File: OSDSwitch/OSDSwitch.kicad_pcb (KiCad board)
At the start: 2 copper layers, 25.4 x 33 mm, 15 parts, among them IC1 ADG1633BCPZ-REEL7, J1 Conn_01x03_Pin, J2 Conn_01x03_Pin, J3 Conn_01x03_Pin, J4 Conn_01x05, J5 Conn_01x04, J6 Conn_01x02

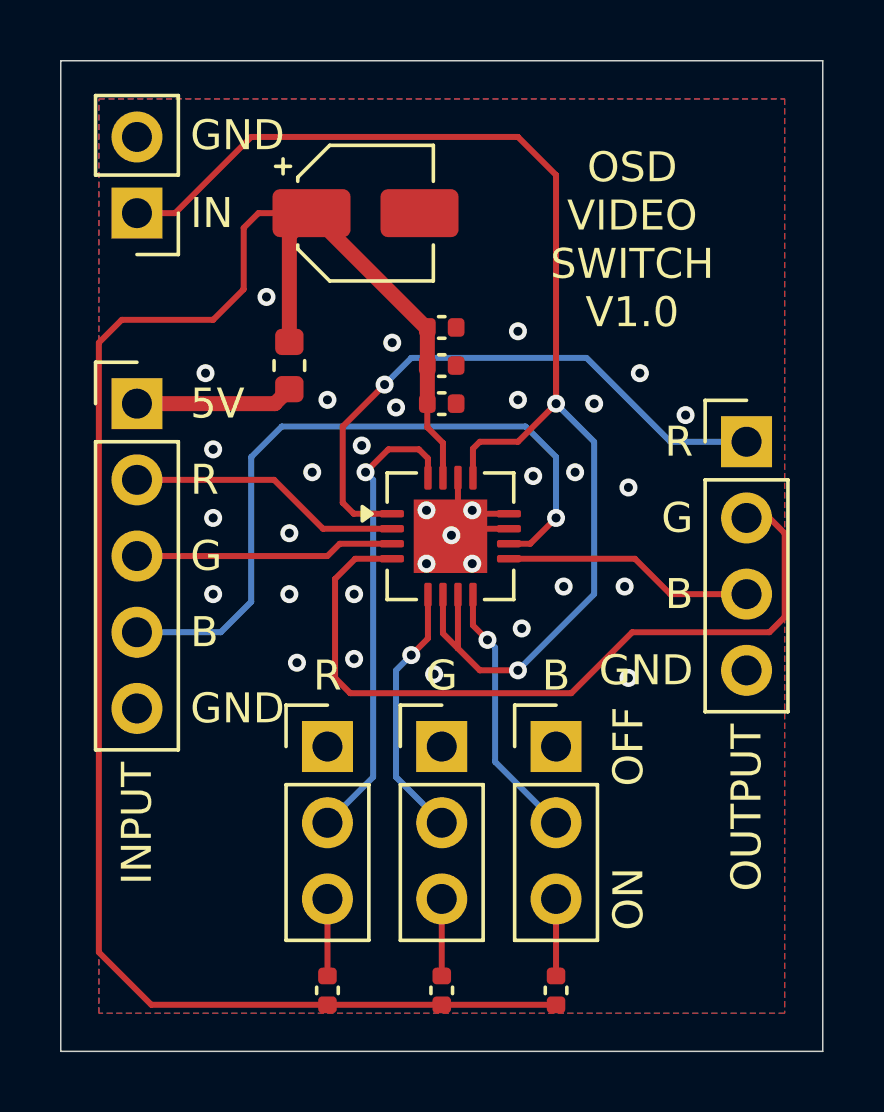
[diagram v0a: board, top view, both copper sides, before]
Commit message: Corrected chip footprint
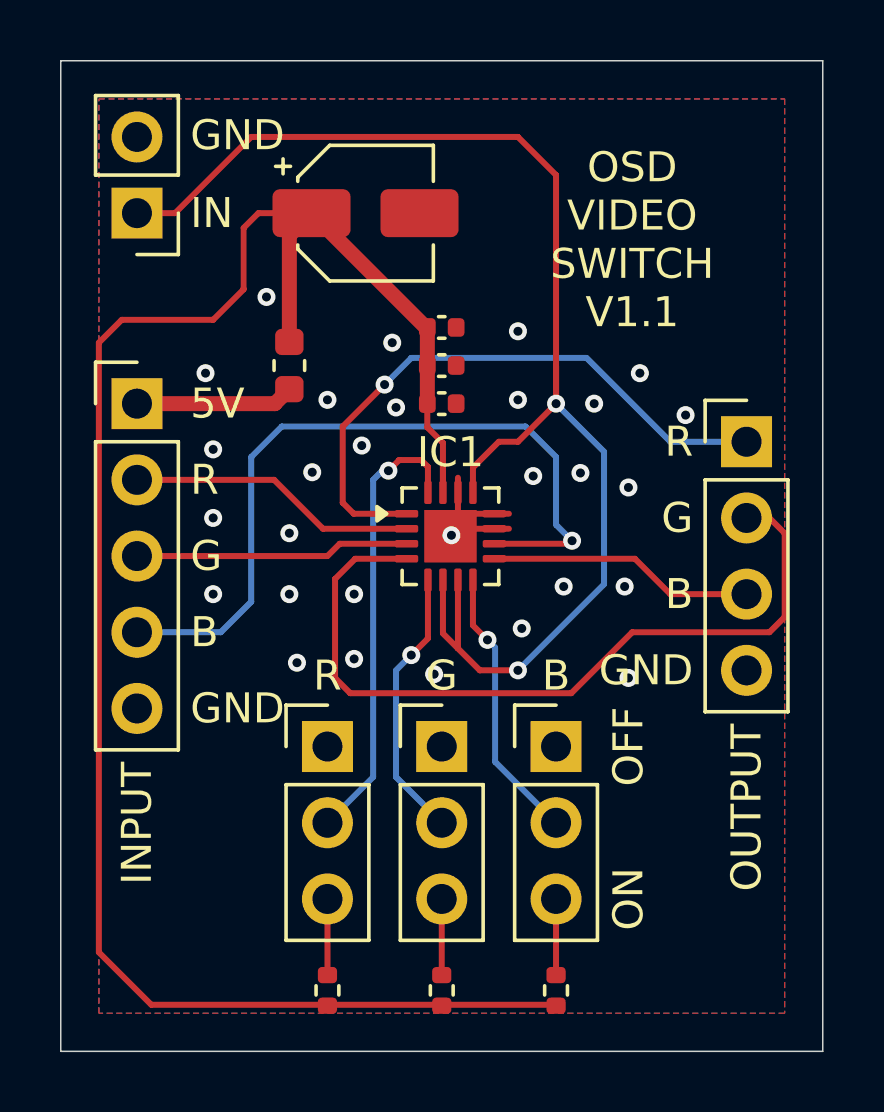
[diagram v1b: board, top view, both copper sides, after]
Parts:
- C4: value 1uF -> 1uF/16V
- IC1: footprint Package_DFN_QFN:QFN-16-1EP_4x4mm_P0.5mm_EP2.45x2.45mm -> Package_DFN_QFN:QFN-16-1EP_3x3mm_P0.5mm_EP1.75x1.75mm
- J1, J3: value Conn_01x03_Pin -> Conn_01x03_Pin_J12
- J2: value Conn_01x03_Pin -> Conn_01x03_Pin_J23
- R1, R2, R3: footprint Capacitor_SMD:C_0402_1005Metric -> Resistor_SMD:R_0402_1005Metric
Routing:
- net /BLUE_IN: track 24.3 -> 26.0 mm
- net /OSD_VID: track 45.4 -> 46.7 mm
- net +5V: track 62.1 -> 63.0 mm
- net GND: vias 33 -> 29
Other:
- board text added: "OSD VIDEO SWITCH V1.1"
- board text removed: "OSD VIDEO SWITCH V1.0"

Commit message: Swapped red and blue to match Amiga 500 video output order
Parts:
- R1, R2, R3: value 470R -> 330R
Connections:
- IC1 pad 1: /RED_OUT -> /BLUE_OUT
- IC1 pad 10: /BLUE_IN -> /RED_IN
- IC1 pad 2: /RED_IN -> /BLUE_IN
- IC1 pad 9: /BLUE_OUT -> /RED_OUT
- J4 pad 2: /RED_IN -> /BLUE_IN
- J4 pad 4: /BLUE_IN -> /RED_IN
- J5 pad 1: /RED_OUT -> /BLUE_OUT
- J5 pad 3: /BLUE_OUT -> /RED_OUT
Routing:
- net /RED_IN: track 9.66 -> 26.0 mm, vias 0 -> 1
- net /BLUE_IN: track 26.0 -> 9.66 mm, vias 1 -> 0
- net /RED_OUT: track 20.4 -> 8.90 mm, vias 1 -> 0
- net /BLUE_OUT: track 8.90 -> 20.4 mm, vias 0 -> 1
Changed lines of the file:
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@@
 			(layers "*.Cu" "*.Mask")
 			(remove_unused_layers no)
-			(net 4 "/RED_IN")
+			(net 12 "/BLUE_IN")
 			(pinfunction "Pin_2")
 			(pintype "passive")
@@
 			(layers "*.Cu" "*.Mask")
 			(remove_unused_layers no)
-			(net 12 "/BLUE_IN")
+			(net 4 "/RED_IN")
 			(pinfunction "Pin_4")
 			(pintype "passive")
@@
 			)
 		)
-		(property "Value" "470R"
+		(property "Value" "330R"
 			(at 0 1.17 90)
 			(layer "F.Fab")
@@
 			)
 		)
-		(property "Value" "470R"
+		(property "Value" "330R"
 			(at 0 1.17 90)
 			(layer "F.Fab")
@@
 			(layers "*.Cu" "*.Mask")
 			(remove_unused_layers no)
-			(net 11 "/RED_OUT")
+			(net 5 "/BLUE_OUT")
 			(pinfunction "Pin_1")
 			(pintype "passive")
@@
 			(layers "*.Cu" "*.Mask")
 			(remove_unused_layers no)
-			(net 5 "/BLUE_OUT")
+			(net 11 "/RED_OUT")
 			(pinfunction "Pin_3")
 			(pintype "passive")
@@
 			)
 		)
-		(property "Value" "470R"
+		(property "Value" "330R"
 			(at 0 1.17 90)
 			(layer "F.Fab")
@@
 			(layers "F.Cu" "F.Mask" "F.Paste")
 			(roundrect_rratio 0.25)
-			(net 11 "/RED_OUT")
+			(net 5 "/BLUE_OUT")
 			(pinfunction "D1")
 			(pintype "passive")
@@
 			(layers "F.Cu" "F.Mask" "F.Paste")
 			(roundrect_rratio 0.25)
-			(net 4 "/RED_IN")
+			(net 12 "/BLUE_IN")
 			(pinfunction "S1B")
 			(pintype "passive")
@@
 			(layers "F.Cu" "F.Mask" "F.Paste")
 			(roundrect_rratio 0.25)
-			(net 5 "/BLUE_OUT")
+			(net 11 "/RED_OUT")
 			(pinfunction "D3")
 			(pintype "passive")
@@
 			(layers "F.Cu" "F.Mask" "F.Paste")
 			(roundrect_rratio 0.25)
-			(net 12 "/BLUE_IN")
+			(net 4 "/RED_IN")
 			(pinfunction "S3B")
 			(pintype "passive")
@@
 	)
 	(gr_text "R"
-		(at 173.482 91.44 0)
+		(at 173.5074 96.52 0)
 		(layer "F.SilkS")
 		(effects
@@
 	)
 	(gr_text "B"
-		(at 173.482 96.52 0)
+		(at 173.5074 91.44 0)
 		(layer "F.SilkS")
 		(effects
@@
 	)
 	(gr_text "B"
-		(at 168.91 99.822 0)
+		(at 161.29 99.822 0)
 		(layer "F.SilkS")
 		(effects
@@
 	)
 	(gr_text "B"
-		(at 156.718 97.79 0)
+		(at 156.718 92.71 0)
 		(layer "F.SilkS")
 		(effects
@@
 	)
 	(gr_text "R"
-		(at 161.29 99.822 0)
+		(at 168.91 99.822 0)
 		(layer "F.SilkS")
 		(effects
@@
 	)
 	(gr_text "R"
-		(at 156.718 92.71 0)
+		(at 156.718 97.7646 0)
 		(layer "F.SilkS")
 		(effects
@@
 	)
 	(segment
-		(start 154.94 92.71)
-		(end 159.512 92.71)
+		(start 169.3434 94.84)
+		(end 166.8525 94.84)
 		(width 0.2)
 		(layer "F.Cu")
@@
 	)
 	(segment
-		(start 159.512 92.71)
-		(end 161.142 94.34)
+		(start 169.4434 94.74)
+		(end 169.3434 94.84)
 		(width 0.2)
 		(layer "F.Cu")
 		(net 4)
 	)
+	(via
+		(at 169.4434 94.74)
+		(size 0.6)
+		(drill 0.3)
+		(layers "F.Cu" "B.Cu")
+		(net 4)
+	)
 	(segment
-		(start 161.142 94.34)
-		(end 163.9275 94.34)
+		(start 158.75 91.948)
+		(end 158.75 96.774)
 		(width 0.2)
-		(layer "F.Cu")
+		(layer "B.Cu")
 		(net 4)
 	)
 	(segment
-		(start 171.54 95.34)
-		(end 172.72 96.52)
+		(start 168.91 94.2066)
+		(end 168.91 91.948)
+		(width 0.2)
+		(layer "B.Cu")
+		(net 4)
+	)
+	(segment
+		(start 154.94 97.536)
+		(end 154.94 97.79)
+		(width 0.2)
+		(layer "B.Cu")
+		(net 4)
+	)
+	(segment
+		(start 169.4434 94.74)
+		(end 168.91 94.2066)
+		(width 0.2)
+		(layer "B.Cu")
+		(net 4)
+	)
+	(segment
+		(start 168.91 91.948)
+		(end 167.894 90.932)
+		(width 0.2)
+		(layer "B.Cu")
+		(net 4)
+	)
+	(segment
+		(start 157.734 97.79)
+		(end 154.94 97.79)
+		(width 0.2)
+		(layer "B.Cu")
+		(net 4)
+	)
+	(segment
+		(start 158.75 96.774)
+		(end 157.734 97.79)
+		(width 0.2)
+		(layer "B.Cu")
+		(net 4)
+	)
+	(segment
+		(start 159.766 90.932)
+		(end 158.75 91.948)
+		(width 0.2)
+		(layer "B.Cu")
+		(net 4)
+	)
+	(segment
+		(start 167.894 90.932)
+		(end 159.766 90.932)
+		(width 0.2)
+		(layer "B.Cu")
+		(net 4)
+	)
+	(segment
+		(start 162.166 93.84)
+		(end 163.9275 93.84)
 		(width 0.2)
 		(layer "F.Cu")
@@
 	)
 	(segment
-		(start 172.72 96.52)
-		(end 175.26 96.52)
+		(start 161.798 93.472)
+		(end 162.166 93.84)
 		(width 0.2)
 		(layer "F.Cu")
@@
 	)
 	(segment
-		(start 166.8525 95.34)
-		(end 171.54 95.34)
+		(start 163.195 89.535)
+		(end 161.798 90.932)
+		(width 0.2)
+		(layer "F.Cu")
+		(net 5)
+	)
+	(segment
+		(start 161.798 90.932)
+		(end 161.798 93.472)
 		(width 0.2)
 		(layer "F.Cu")
 		(net 5)
 	)
+	(via
+		(at 163.195 89.535)
+		(size 0.6)
+		(drill 0.3)
+		(layers "F.Cu" "B.Cu")
+		(net 5)
+	)
+	(segment
+		(start 172.72 91.44)
+		(end 175.26 91.44)
+		(width 0.2)
+		(layer "B.Cu")
+		(net 5)
+	)
+	(segment
+		(start 164.084 88.646)
+		(end 169.926 88.646)
+		(width 0.2)
+		(layer "B.Cu")
+		(net 5)
+	)
+	(segment
+		(start 169.926 88.646)
+		(end 172.72 91.44)
+		(width 0.2)
+		(layer "B.Cu")
+		(net 5)
+	)
+	(segment
+		(start 163.195 89.535)
+		(end 164.084 88.646)
+		(width 0.2)
+		(layer "B.Cu")
+		(net 5)
+	)
 	(segment
 		(start 164.64 96.0525)
@@
 	)
 	(segment
-		(start 162.166 93.84)
-		(end 163.9275 93.84)
+		(start 171.54 95.34)
+		(end 172.72 96.52)
 		(width 0.2)
 		(layer "F.Cu")
@@
 	)
 	(segment
-		(start 161.798 93.472)
-		(end 162.166 93.84)
+		(start 172.72 96.52)
+		(end 175.26 96.52)
 		(width 0.2)
 		(layer "F.Cu")
@@
 	)
 	(segment
-		(start 163.195 89.535)
-		(end 161.798 90.932)
+		(start 166.8525 95.34)
+		(end 171.54 95.34)
 		(width 0.2)
 		(layer "F.Cu")
@@
 	)
 	(segment
-		(start 161.798 90.932)
-		(end 161.798 93.472)
-		(width 0.2)
-		(layer "F.Cu")
-		(net 11)
-	)
-	(via
-		(at 163.195 89.535)
-		(size 0.6)
-		(drill 0.3)
-		(layers "F.Cu" "B.Cu")
-		(net 11)
-	)
-	(segment
-		(start 172.72 91.44)
-		(end 175.26 91.44)
-		(width 0.2)
-		(layer "B.Cu")
-		(net 11)
-	)
-	(segment
-		(start 164.084 88.646)
-		(end 169.926 88.646)
-		(width 0.2)
-		(layer "B.Cu")
-		(net 11)
-	)
-	(segment
-		(start 169.926 88.646)
-		(end 172.72 91.44)
-		(width 0.2)
-		(layer "B.Cu")
-		(net 11)
-	)
-	(segment
-		(start 163.195 89.535)
-		(end 164.084 88.646)
-		(width 0.2)
-		(layer "B.Cu")
-		(net 11)
-	)
-	(segment
-		(start 169.3434 94.84)
-		(end 166.8525 94.84)
+		(start 154.94 92.71)
+		(end 159.512 92.71)
 		(width 0.2)
 		(layer "F.Cu")
@@
 	)
 	(segment
-		(start 169.4434 94.74)
-		(end 169.3434 94.84)
+		(start 159.512 92.71)
+		(end 161.142 94.34)
 		(width 0.2)
 		(layer "F.Cu")
 		(net 12)
 	)
-	(via
-		(at 169.4434 94.74)
-		(size 0.6)
-		(drill 0.3)
-		(layers "F.Cu" "B.Cu")
-		(net 12)
-	)
-	(segment
-		(start 158.75 91.948)
-		(end 158.75 96.774)
-		(width 0.2)
-		(layer "B.Cu")
-		(net 12)
-	)
-	(segment
-		(start 168.91 94.2066)
-		(end 168.91 91.948)
-		(width 0.2)
-		(layer "B.Cu")
-		(net 12)
-	)
-	(segment
-		(start 154.94 97.536)
-		(end 154.94 97.79)
-		(width 0.2)
-		(layer "B.Cu")
-		(net 12)
-	)
 	(segment
-		(start 169.4434 94.74)
-		(end 168.91 94.2066)
-		(width 0.2)
-		(layer "B.Cu")
-		(net 12)
-	)
-	(segment
-		(start 168.91 91.948)
-		(end 167.894 90.932)
-		(width 0.2)
-		(layer "B.Cu")
-		(net 12)
-	)
-	(segment
-		(start 157.734 97.79)
-		(end 154.94 97.79)
-		(width 0.2)
-		(layer "B.Cu")
-		(net 12)
-	)
-	(segment
-		(start 158.75 96.774)
-		(end 157.734 97.79)
-		(width 0.2)
-		(layer "B.Cu")
-		(net 12)
-	)
-	(segment
-		(start 159.766 90.932)
-		(end 158.75 91.948)
-		(width 0.2)
-		(layer "B.Cu")
-		(net 12)
-	)
-	(segment
-		(start 167.894 90.932)
-		(end 159.766 90.932)
+		(start 161.142 94.34)
+		(end 163.9275 94.34)
 		(width 0.2)
-		(layer "B.Cu")
+		(layer "F.Cu")
 		(net 12)
 	)
